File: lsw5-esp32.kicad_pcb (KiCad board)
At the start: 2 copper layers, 35 x 52 mm, 32 parts, among them J1 Conn_02x03_Odd_Even, J2 Conn_01x04_Pin, J3 USB4105-GF-A, J4 Conn_02x05_Odd_Even, J5 Conn_01x03, Q1 AO3407A, U1 ESP32-S3-WROOM-1U, U2 LD1117S33TR_SOT223, U3 SP3485EN

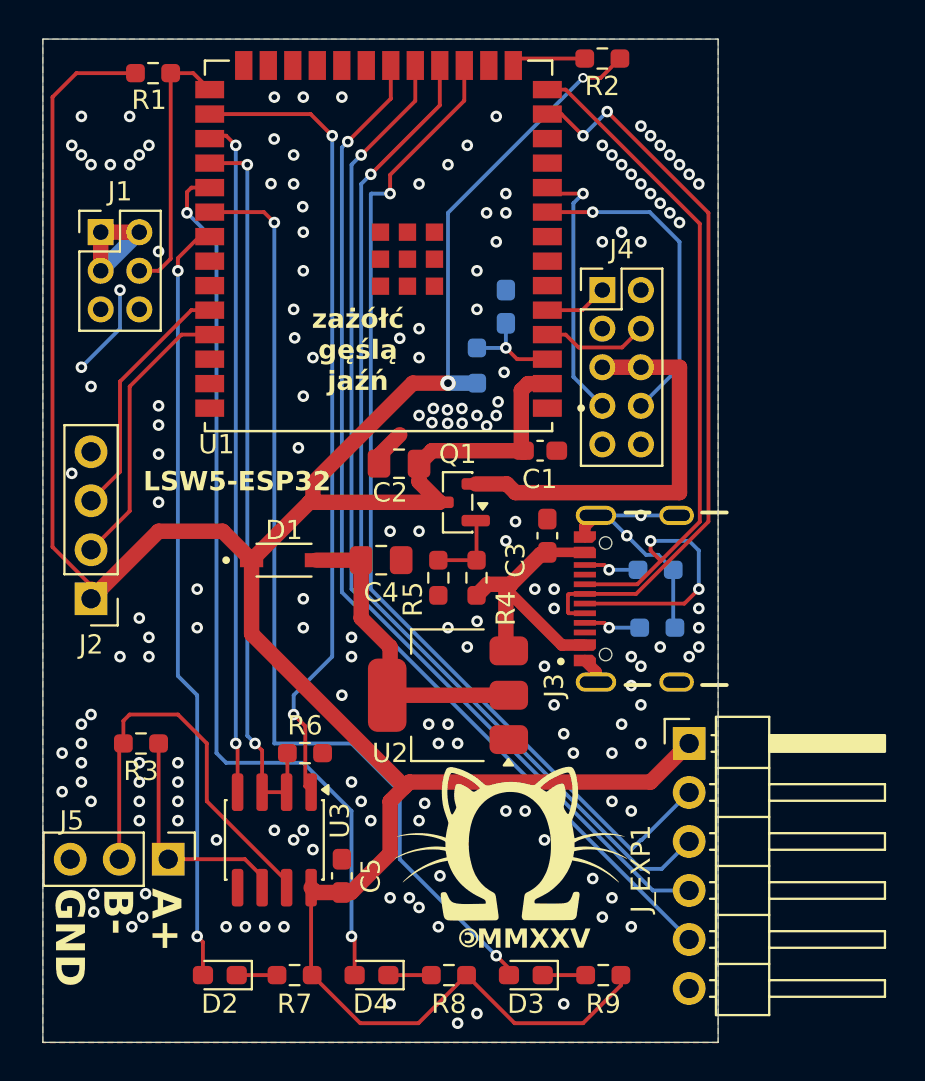
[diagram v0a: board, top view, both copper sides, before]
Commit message: increase a few clearances
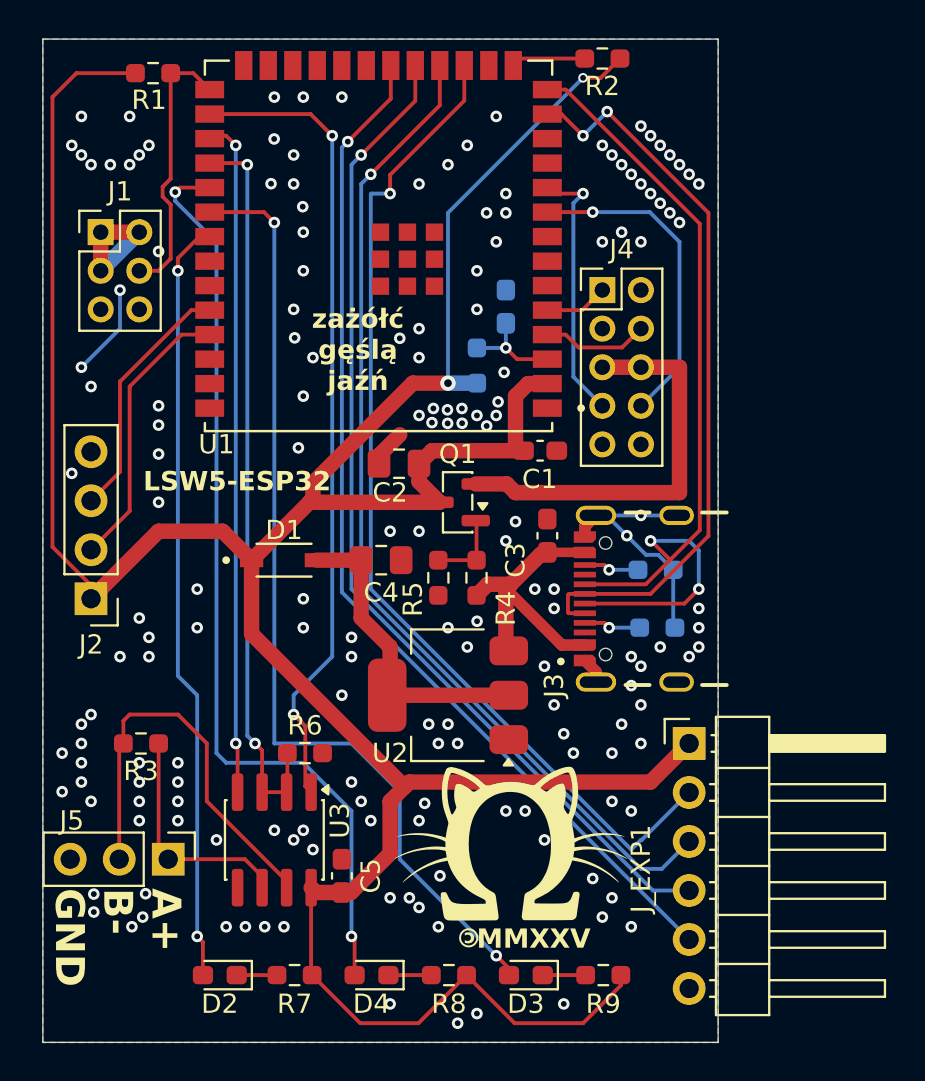
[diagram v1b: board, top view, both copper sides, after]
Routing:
- net /Net-(D2-A): track 47.8 -> 48.7 mm
- net /Net-(J4-Pin_1): track 11.4 -> 10.7 mm

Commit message: Fix swapped LED labels
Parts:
- D2: value RDY -> COM
- D3: value COM -> RDY
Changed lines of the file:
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@@
 			)
 		)
-		(property "Value" "RDY"
+		(property "Value" "COM"
 			(at 0 1.43 0)
 			(layer "F.Fab")
@@
 			)
 		)
-		(property "Value" "COM"
+		(property "Value" "RDY"
 			(at 0 1.43 0)
 			(layer "F.Fab")

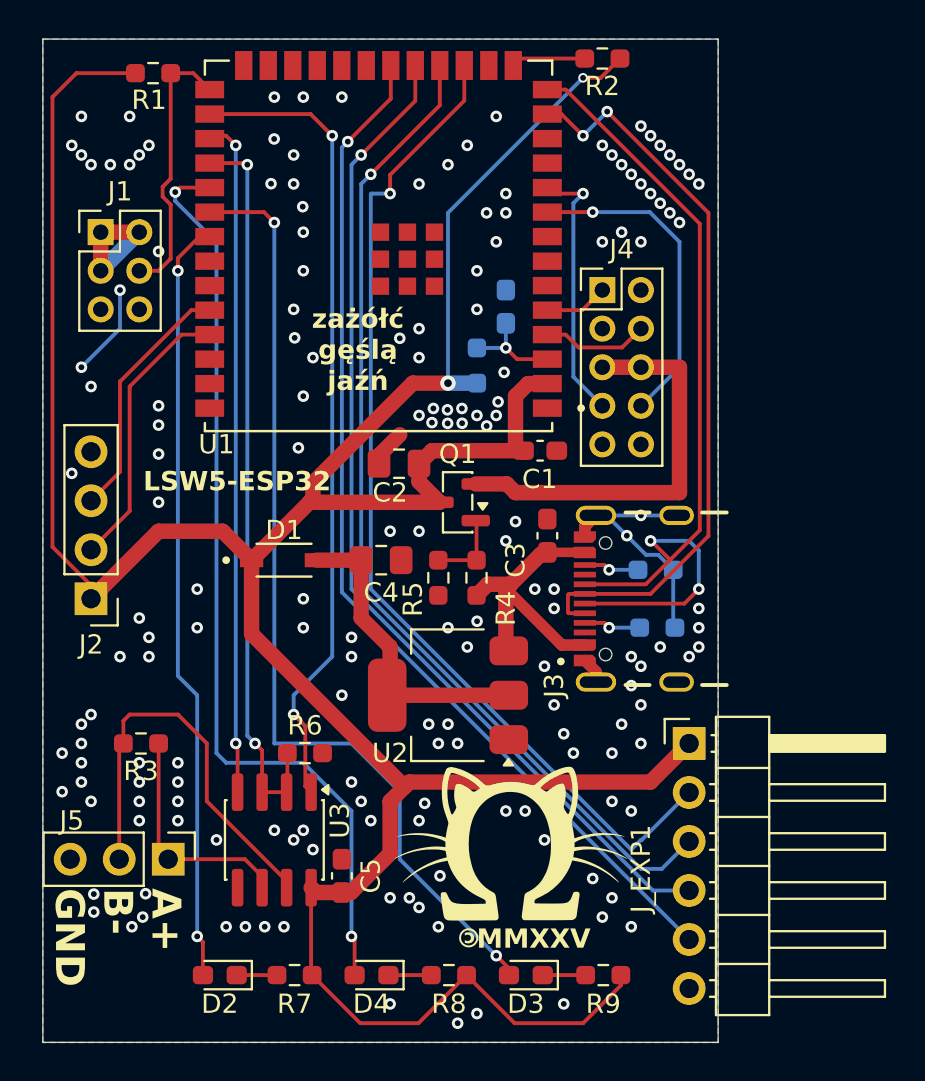
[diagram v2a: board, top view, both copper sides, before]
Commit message: Move RS485 transceiver off octal SPI pins
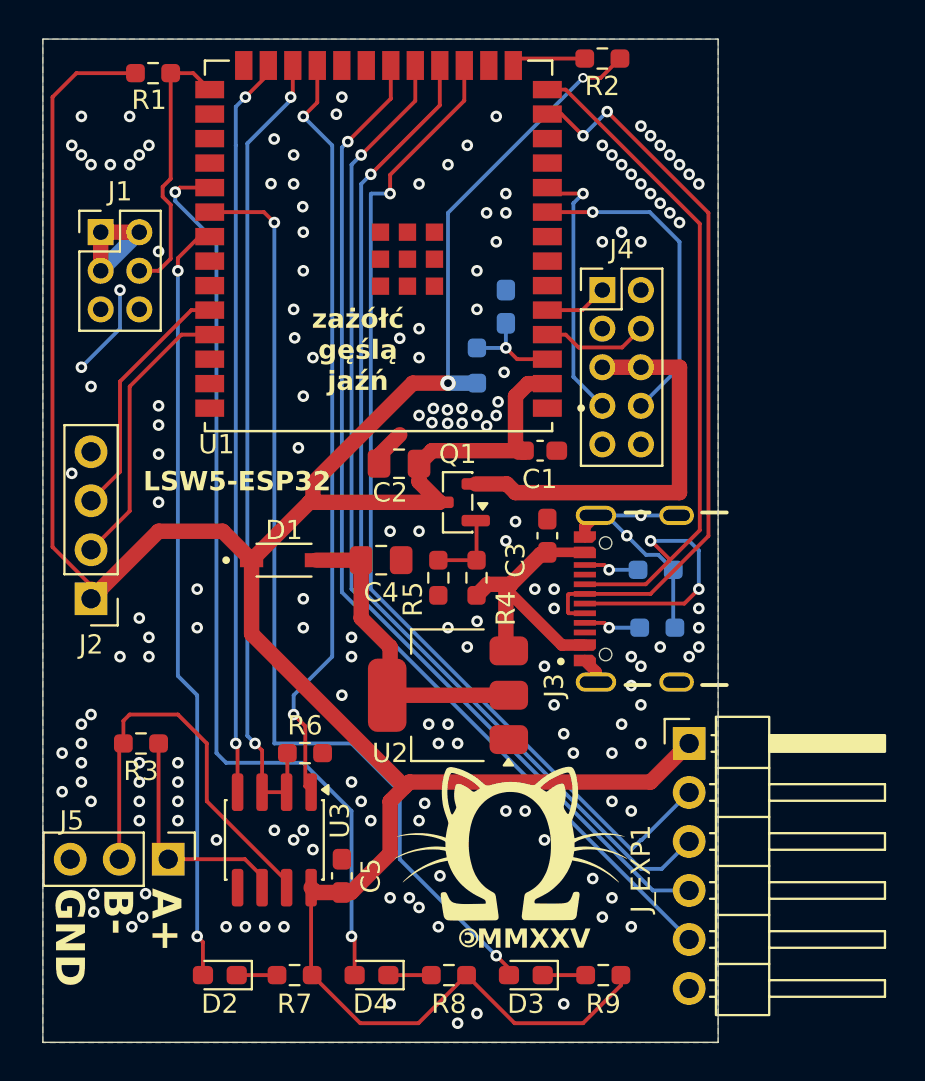
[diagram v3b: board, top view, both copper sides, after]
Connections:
- R6 pad 1: Net-(U1-IO37) -> Net-(U1-IO47)
- U1 pad 23: unconnected-(U1-IO21-Pad23) -> Net-(U1-IO21)
- U1 pad 24: unconnected-(U1-IO47-Pad24) -> Net-(U1-IO47)
- U1 pad 25: unconnected-(U1-IO48-Pad25) -> Net-(U1-IO48)
- U1 pad 28: Net-(U1-IO35) -> unconnected-(U1-IO35-Pad28)
- U1 pad 29: Net-(U1-IO36) -> unconnected-(U1-IO36-Pad29)
- U1 pad 30: Net-(U1-IO37) -> unconnected-(U1-IO37-Pad30)
- U3 pad 1: Net-(U1-IO35) -> Net-(U1-IO21)
- U3 pad 2: Net-(U1-IO37) -> Net-(U1-IO47)
- U3 pad 3: Net-(U1-IO37) -> Net-(U1-IO47)
- U3 pad 4: Net-(U1-IO36) -> Net-(U1-IO48)
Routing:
- net Net-(U1-IO47): track 0.00 -> 42.2 mm, vias 0 -> 2
- net Net-(U1-IO35): track 42.0 -> 0.00 mm, vias 2 -> 0
- net Net-(U1-IO21): track 0.00 -> 39.8 mm, vias 0 -> 2
- net Net-(U1-IO48): track 0.00 -> 38.4 mm, vias 0 -> 2
- net Net-(U1-IO37): track 38.1 -> 0.00 mm, vias 2 -> 0
- net Net-(U1-IO36): track 35.0 -> 0.00 mm, vias 2 -> 0
- net GND: vias 173 -> 172

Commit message: Add p1 label
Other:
- board text added: "p1"
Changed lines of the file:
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@@
+		)
+	)
+	(gr_text "p1"
+		(at 6.5 26 0)
+		(layer "F.SilkS")
+		(effects
+			(font
+				(size 1 1)
+				(thickness 0.2)
+				(bold yes)
+			)
+			(justify left bottom)
 		)
 	)

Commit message: Fix fp path, centralise PWR_FLAG
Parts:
- U1: footprint lsw5-esp32:ESP32-S3-WROOM-1U-N16R8 -> ESP32-S3-WROOM-1U:ESP32-S3-WROOM-1U-N16R8
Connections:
- J1 pad 5: /unconnected-(J2-Pin_5-Pad5) -> unconnected-(J1-Pin_5-Pad5)
- J1 pad 6: /unconnected-(J2-Pin_6-Pad6) -> unconnected-(J1-Pin_6-Pad6)
- J4 pad 2: /unconnected-(J1-Pin_2-Pad2) -> unconnected-(J4-Pin_2-Pad2)
- J4 pad 3: /unconnected-(J1-Pin_3-Pad3) -> unconnected-(J4-Pin_3-Pad3)

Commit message: p1 isolate RS485 transceiver
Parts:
- removed J5: Conn_01x03, Connector_PinHeader_2.54mm:PinHeader_1x03_P2.54mm_Vertical
- added C7: 100n, Capacitor_SMD:C_0603_1608Metric_Pad1.08x0.95mm_HandSolder, F.Cu at (13.3, 42.3)
- added C8: 10μ, Capacitor_SMD:C_0805_2012Metric_Pad1.18x1.45mm_HandSolder, F.Cu at (13.4, 44.1)
- added D5: SM712_SOT23, Package_TO_SOT_SMD:SOT-23, F.Cu at (9.65, 45.0)
- added J6: Conn_01x04, Connector_PinHeader_2.54mm:PinHeader_1x04_P2.54mm_Vertical, F.Cu at (2.38, 37.5)
- added R13: 10, Resistor_SMD:R_0603_1608Metric_Pad0.98x0.95mm_HandSolder, F.Cu at (6.29, 45.4)
- R6: value 10k -> 10
- U3: value SP3485EN -> ISO1410DWR; footprint Package_SO:SOIC-8_3.9x4.9mm_P1.27mm -> ISO1410DWR:SOIC127P1030X265-16N
- moved C5 11.6 mm to (15.8, 32.8), turned to -90 degrees
- moved R6 8.47 mm to (6.33, 42.4), turned to 180 degrees
- moved U3 7.23 mm to (9.60, 35.7)
- moved R3 6.67 mm to (9.65, 42.4), turned to 0 degrees
- moved J2 4.00 mm to (2.50, 26.0)
- moved C2 2.62 mm to (21.1, 22.6)
- moved U2 1.90 mm to (22.8, 34.2)
- moved C1 1.16 mm to (24.6, 22.3)
- moved D1 0.60 mm to (13.1, 28.0)
- moved Q1 0.40 mm to (21.5, 25.4)
- moved R4 0.16 mm to (22.5, 28.8)
- moved R5 0.16 mm to (20.5, 28.8)
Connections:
- R3 pad 1: Net-(J5-Pin_1) -> Net-(D5-A2)
- R3 pad 2: Net-(J5-Pin_2) -> Net-(D5-A1)
- R6 pad 1: Net-(U1-IO47) -> Net-(D5-A2)
- R6 pad 2: GND -> Net-(J6-Pin_3)
- U1 pad 23: Net-(U1-IO21) -> /RX_RS485
- U1 pad 24: Net-(U1-IO47) -> /DE_RS485
- U1 pad 25: Net-(U1-IO48) -> /TX_RS485
- U3 pad 1: Net-(U1-IO21) -> +3V3
- U3 pad 2: Net-(U1-IO47) -> GND
- U3 pad 3: Net-(U1-IO47) -> /RX_RS485
- U3 pad 4: Net-(U1-IO48) -> /DE_RS485
- U3 pad 5: GND -> /DE_RS485
- U3 pad 6: Net-(J5-Pin_1) -> /TX_RS485
- U3 pad 7: Net-(J5-Pin_2) -> unconnected-(U3-NC_7-Pad7)
- U3 pad 8: +3V3 -> GND
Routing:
- net Net-(U1-IO47): track 42.2 -> 0.00 mm, vias 2 -> 0
- net Net-(U1-IO21): track 39.8 -> 0.00 mm, vias 2 -> 0
- net Net-(U1-IO48): track 38.4 -> 0.00 mm, vias 2 -> 0
- net /DE_RS485: track 0.00 -> 31.1 mm, vias 0 -> 2
- net /TX_RS485: track 0.00 -> 30.3 mm, vias 0 -> 2
- net /RX_RS485: track 0.00 -> 29.8 mm, vias 0 -> 2
- net Net-(J5-Pin_2): track 20.9 -> 0.00 mm
- net +5V_ISO: track 0.00 -> 18.2 mm
- net Net-(D2-A): track 39.3 -> 55.1 mm
- net Net-(J5-Pin_1): track 10.7 -> 0.00 mm
- net /USB_DP: track 46.2 -> 35.7 mm, vias 2 -> 0
- net +3V3: track 163.2 -> 152.8 mm
- net Net-(D5-A1): track 0.00 -> 7.34 mm
- net Net-(D5-A2): track 0.00 -> 5.03 mm
- net /PRG_TX: track 14.6 -> 10.6 mm
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- added copper zone on B.Cu, net GND_ISO
- added copper zone on F.Cu, net GND_ISO
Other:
- board text added: "5V"
- board text added: "MMXXVI"
- board text removed: "MMXXV"

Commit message: set title and revision
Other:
- board text added: "${REVISION}"
- board text added: "${TITLE}"
- board text removed: "LSW5-ESP32"
- board text removed: "p1"
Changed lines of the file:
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@@
 	)
 	(paper "A4")
+	(title_block
+		(title "LSW5-ESP32")
+		(rev "p1")
+	)
 	(layers
 		(0 "F.Cu" signal)
@@
 		)
 	)
-	(gr_text "p1"
+	(gr_text "${REVISION}"
 		(at 6.5 26 0)
 		(layer "F.SilkS")
@@
 		)
 	)
-	(gr_text "LSW5-ESP32"
+	(gr_text "${TITLE}"
 		(at 5.201088 24.499999 0)
 		(layer "F.SilkS")

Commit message: improve noise immunity of power switch
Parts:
- R5: value 100k -> 10k
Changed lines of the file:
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@@
 			)
 		)
-		(property "Value" "100k"
+		(property "Value" "10k"
 			(at 0 1.43 90)
 			(layer "F.Fab")
